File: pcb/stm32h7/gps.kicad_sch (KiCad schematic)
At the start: 8 parts, among them J3 GPS_ANT, U5 24AA32AF-I_MS

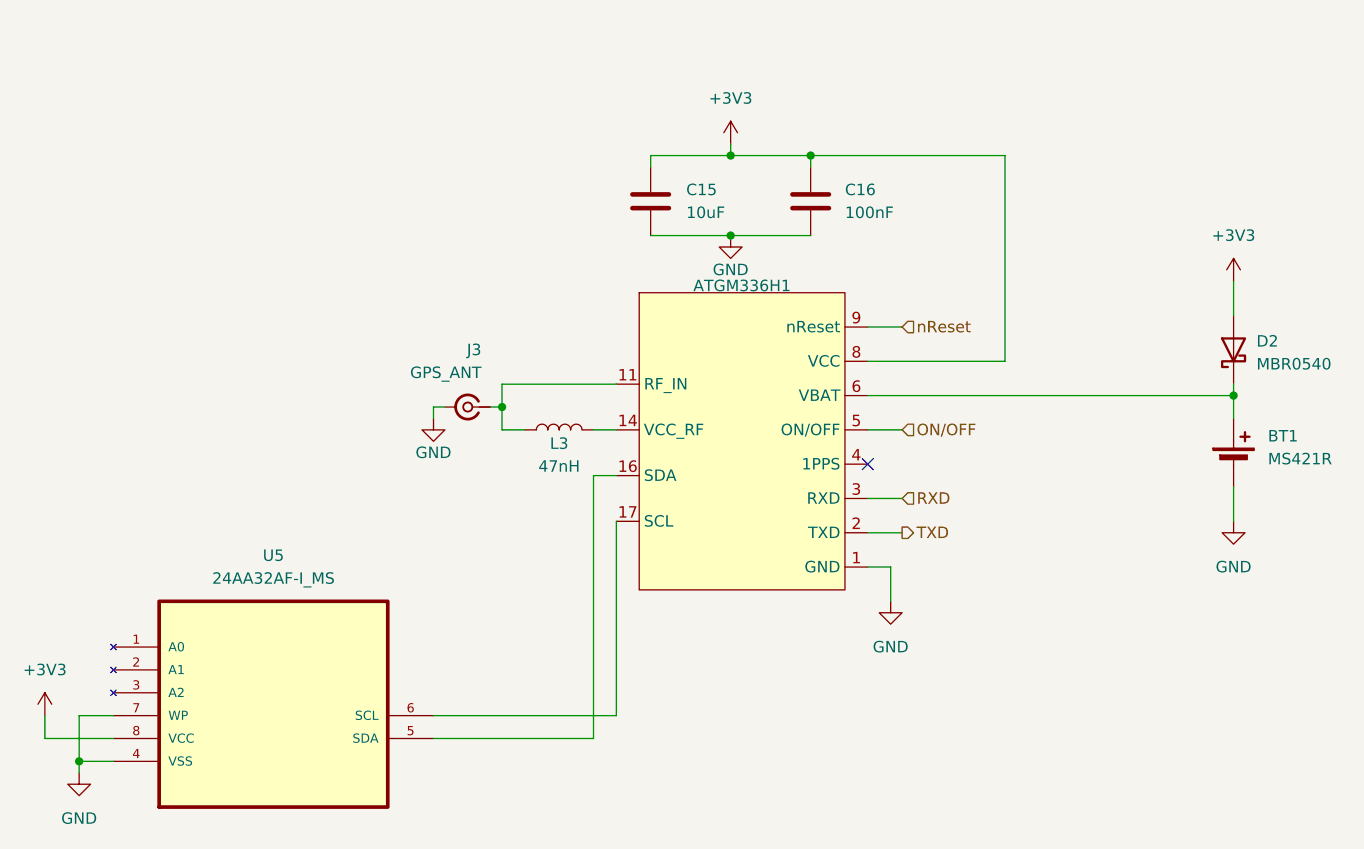
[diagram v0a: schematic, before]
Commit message: fixed some footprints and added power switching mosfet for gps
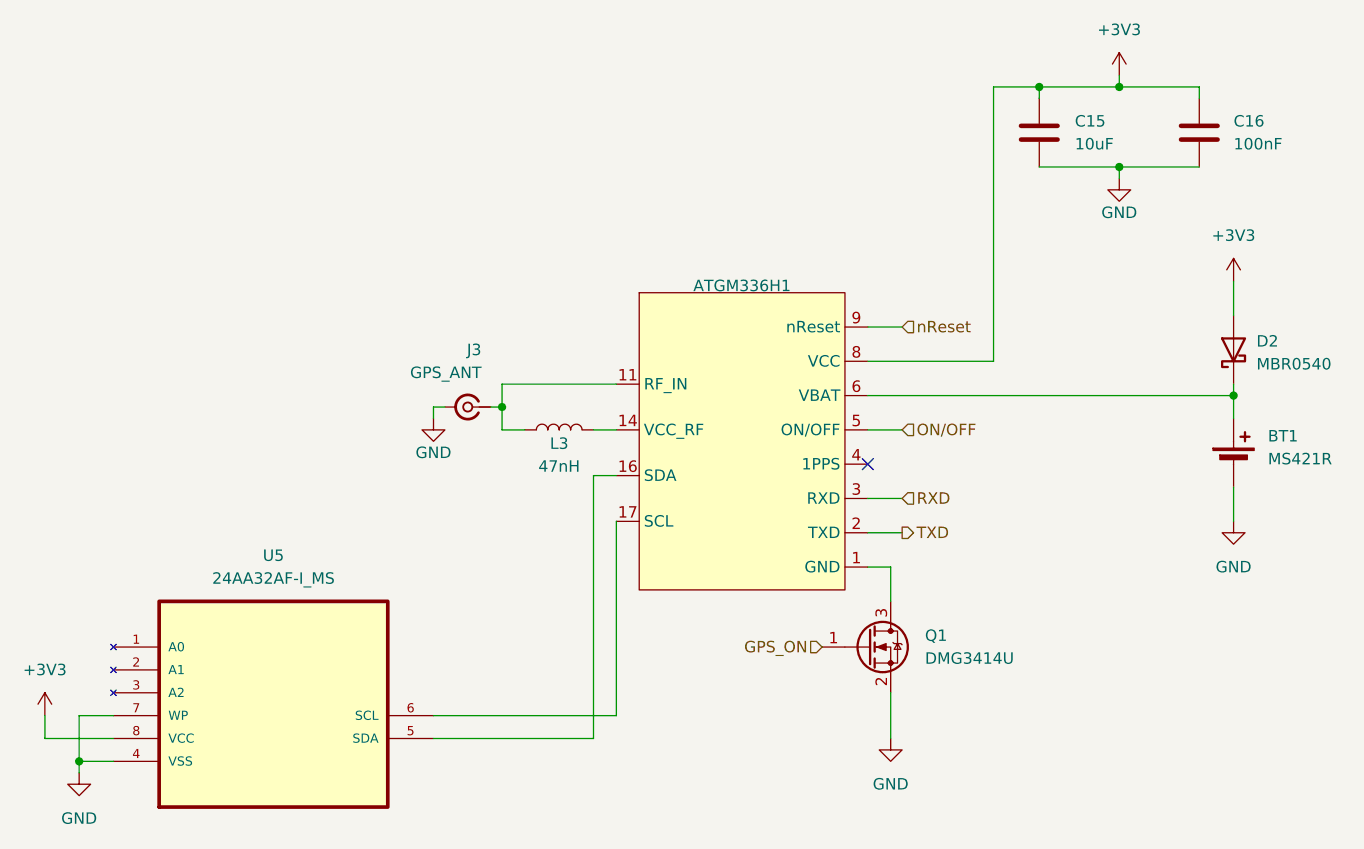
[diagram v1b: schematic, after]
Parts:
- added Q1: DMG3414U, Package_TO_SOT_SMD:SOT-23, symbol Transistor_FET:DMG3414U
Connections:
- net GND: now also Q1.2 (S); no longer ATGM336H1.1 (GND)
- new net: ATGM336H1.1 (GND), Q1.3 (D)
- new net GPS_ON: Q1.1 (G)
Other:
- moved on the sheet: C15, C16
